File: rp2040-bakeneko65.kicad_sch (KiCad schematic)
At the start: 1 part

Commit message: Some schematic work
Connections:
- net +3V3: now reaches U?.1 (IOVDD), U?.10 (IOVDD), U?.22 (IOVDD), U?.33 (IOVDD), U?.42 (IOVDD), U?.49 (IOVDD)
- net +3V3: now also U?.43 (ADC_AVDD), U?.44 (VREG_IN), U?.48 (USB_VDD)
- net +1V1: now reaches U?.23 (DVDD), U?.50 (DVDD)
- net +1V1: now also U?.45 (VREG_VOUT)
- net SWCLK: now reaches U?.24 (SWCLK)
- net SWD: now reaches U?.25 (SWD)
- net SD3: now reaches U?.51 (QSPI_SD3)
- net QSPI_CLK: now reaches U?.52 (QSPI_SCLK)
- net SD0: now reaches U?.53 (QSPI_SD0)
- net SD2: now reaches U?.54 (QSPI_SD2)
- net SD1: now reaches U?.55 (QSPI_SD1)
- net CS: now reaches U?.56 (QSPI_SS)
- net GND: now reaches U?.57 (GND)
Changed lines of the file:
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@@
 (kicad_sch (version 20211123) (generator eeschema)
   (paper "A4")
+  (junction (at 81.28 29.21) (diameter 0) (color 0 0 0 0)
+  )
+  (junction (at 78.74 29.21) (diameter 0) (color 0 0 0 0)
+  )
+  (junction (at 76.2 29.21) (diameter 0) (color 0 0 0 0)
+  )
+  (junction (at 68.58 29.21) (diameter 0) (color 0 0 0 0)
+  )
+  (wire (pts (xy 76.2 29.21) (xy 78.74 29.21))
+    (stroke (width 0) (type default) (color 0 0 0 0))
+  )
+  (wire (pts (xy 76.2 26.67) (xy 76.2 29.21))
+    (stroke (width 0) (type default) (color 0 0 0 0))
+  )
+  (wire (pts (xy 69.85 120.65) (xy 73.66 120.65))
+    (stroke (width 0) (type default) (color 0 0 0 0))
+  )
+  (wire (pts (xy 78.74 29.21) (xy 81.28 29.21))
+    (stroke (width 0) (type default) (color 0 0 0 0))
+  )
+  (wire (pts (xy 68.58 29.21) (xy 71.12 29.21))
+    (stroke (width 0) (type default) (color 0 0 0 0))
+  )
+  (wire (pts (xy 81.28 29.21) (xy 83.82 29.21))
+    (stroke (width 0) (type default) (color 0 0 0 0))
+  )
+  (wire (pts (xy 68.58 26.67) (xy 68.58 29.21))
+    (stroke (width 0) (type default) (color 0 0 0 0))
+  )
+  (global_label "CS" (shape input) (at 48.26 54.61 180) (fields_autoplaced)
+    (effects (font (size 1.27 1.27)) (justify right))
+    (property "Intersheet References" "${INTERSHEET_REFS}" (id 0) (at 43.3674 54.5306 0)
+      (effects (font (size 1.27 1.27)) (justify right) hide)
+    )
+  )
+  (global_label "QSPI_CLK" (shape input) (at 48.26 69.85 180) (fields_autoplaced)
+    (effects (font (size 1.27 1.27)) (justify right))
+    (property "Intersheet References" "${INTERSHEET_REFS}" (id 0) (at 36.8964 69.7706 0)
+      (effects (font (size 1.27 1.27)) (justify right) hide)
+    )
+  )
+  (global_label "SWCLK" (shape input) (at 48.26 102.87 180) (fields_autoplaced)
+    (effects (font (size 1.27 1.27)) (justify right))
+    (property "Intersheet References" "${INTERSHEET_REFS}" (id 0) (at 39.6179 102.7906 0)
+      (effects (font (size 1.27 1.27)) (justify right) hide)
+    )
+  )
+  (global_label "SWD" (shape input) (at 48.26 105.41 180) (fields_autoplaced)
+    (effects (font (size 1.27 1.27)) (justify right))
+    (property "Intersheet References" "${INTERSHEET_REFS}" (id 0) (at 41.9159 105.3306 0)
+      (effects (font (size 1.27 1.27)) (justify right) hide)
+    )
+  )
+  (global_label "SD1" (shape input) (at 48.26 62.23 180) (fields_autoplaced)
+    (effects (font (size 1.27 1.27)) (justify right))
+    (property "Intersheet References" "${INTERSHEET_REFS}" (id 0) (at 42.1579 62.1506 0)
+      (effects (font (size 1.27 1.27)) (justify right) hide)
+    )
+  )
+  (global_label "SD2" (shape input) (at 48.26 64.77 180) (fields_autoplaced)
+    (effects (font (size 1.27 1.27)) (justify right))
+    (property "Intersheet References" "${INTERSHEET_REFS}" (id 0) (at 42.1579 64.6906 0)
+      (effects (font (size 1.27 1.27)) (justify right) hide)
+    )
+  )
+  (global_label "SD0" (shape input) (at 48.26 59.69 180) (fields_autoplaced)
+    (effects (font (size 1.27 1.27)) (justify right))
+    (property "Intersheet References" "${INTERSHEET_REFS}" (id 0) (at 42.1579 59.6106 0)
+      (effects (font (size 1.27 1.27)) (justify right) hide)
+    )
+  )
+  (global_label "SD3" (shape input) (at 48.26 67.31 180) (fields_autoplaced)
+    (effects (font (size 1.27 1.27)) (justify right))
+    (property "Intersheet References" "${INTERSHEET_REFS}" (id 0) (at 42.1579 67.2306 0)
+      (effects (font (size 1.27 1.27)) (justify right) hide)
+    )
+  )
+  (symbol (lib_id "power:GND") (at 69.85 120.65 0) (unit 1)
+    (in_bom yes) (on_board yes) (fields_autoplaced)
+    (property "Reference" "#PWR?" (id 0) (at 69.85 127 0)
+      (effects (font (size 1.27 1.27)) hide)
+    )
+    (property "Value" "GND" (id 1) (at 69.85 125.73 0))
+    (property "Footprint" "" (id 2) (at 69.85 120.65 0)
+      (effects (font (size 1.27 1.27)) hide)
+    )
+    (property "Datasheet" "" (id 3) (at 69.85 120.65 0)
+      (effects (font (size 1.27 1.27)) hide)
+    )
+    (pin "1")
+  )
+  (symbol (lib_id "power:+3V3") (at 76.2 26.67 0) (unit 1)
+    (in_bom yes) (on_board yes) (fields_autoplaced)
+    (property "Reference" "#PWR?" (id 0) (at 76.2 30.48 0)
+      (effects (font (size 1.27 1.27)) hide)
+    )
+    (property "Value" "+3V3" (id 1) (at 76.2 21.59 0))
+    (property "Footprint" "" (id 2) (at 76.2 26.67 0)
+      (effects (font (size 1.27 1.27)) hide)
+    )
+    (property "Datasheet" "" (id 3) (at 76.2 26.67 0)
+      (effects (font (size 1.27 1.27)) hide)
+    )
+    (pin "1")
+  )
   (symbol (lib_id "MCU_RaspberryPi:RP2040") (at 73.66 74.93 0) (unit 1)
     (in_bom yes) (on_board yes) (fields_autoplaced)
@@
     (pin "9")
   )
+  (symbol (lib_id "power:+1V1") (at 68.58 26.67 0) (unit 1)
+    (in_bom yes) (on_board yes) (fields_autoplaced)
+    (property "Reference" "#PWR?" (id 0) (at 68.58 30.48 0)
+      (effects (font (size 1.27 1.27)) hide)
+    )
+    (property "Value" "+1V1" (id 1) (at 68.58 21.59 0))
+    (property "Footprint" "" (id 2) (at 68.58 26.67 0)
+      (effects (font (size 1.27 1.27)) hide)
+    )
+    (property "Datasheet" "" (id 3) (at 68.58 26.67 0)
+      (effects (font (size 1.27 1.27)) hide)
+    )
+    (pin "1")
+  )
   (sheet_instances
     (path "/" (page "1"))
   )
   (symbol_instances
+    (path "/0429f72c-16b0-4744-90f4-bc022597ca0f"
+      (reference "#PWR?") (unit 1) (value "GND") (footprint "")
+    )
+    (path "/10a7cbd1-d76a-46cc-8e26-d9c6917c2458"
+      (reference "#PWR?") (unit 1) (value "+3V3") (footprint "")
+    )
+    (path "/7e675cbf-1df0-4184-8643-46226909b2bc"
+      (reference "#PWR?") (unit 1) (value "+1V1") (footprint "")
+    )
     (path "/7983fcb6-a16e-4782-bd80-c146df78a95c"
       (reference "U?") (unit 1) (value "RP2040") (footprint "Package_DFN_QFN:QFN-56-1EP_7x7mm_P0.4mm_EP3.2x3.2mm")

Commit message: MCU done
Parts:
- added R5, R6: 27, symbol Device:R_Small
- added R7: 10k, symbol Device:R_Small
- added SW?: SW_Push, symbol Switch:SW_Push
- gave numbers to parts that had none: 1
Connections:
- net GND: now also U3.19 (TESTEN), SW?.1
- net XTAL_IN: now reaches U3.20 (XIN)
- net XTAL_OUT: now reaches U3.21 (XOUT)
- net at U3.26 (RUN): now also R7.2, SW?.2
- net at U3.46 (USB_DM): now also R6.2
- net at U3.47 (USB_DP): now also R5.2
- new net +5V: R7.1
- new net D+: R5.1
- new net D-: R6.1
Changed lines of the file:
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@@
   (junction (at 76.2 29.21) (diameter 0) (color 0 0 0 0)
   )
+  (junction (at 46.99 36.83) (diameter 0) (color 0 0 0 0)
+  )
   (junction (at 68.58 29.21) (diameter 0) (color 0 0 0 0)
   )
@@
     (stroke (width 0) (type default) (color 0 0 0 0))
   )
+  (wire (pts (xy 45.72 82.55) (xy 48.26 82.55))
+    (stroke (width 0) (type default) (color 0 0 0 0))
+  )
   (wire (pts (xy 69.85 120.65) (xy 73.66 120.65))
     (stroke (width 0) (type default) (color 0 0 0 0))
@@
     (stroke (width 0) (type default) (color 0 0 0 0))
   )
+  (wire (pts (xy 46.99 31.75) (xy 46.99 36.83))
+    (stroke (width 0) (type default) (color 0 0 0 0))
+  )
+  (wire (pts (xy 34.29 35.56) (xy 30.48 35.56))
+    (stroke (width 0) (type default) (color 0 0 0 0))
+  )
+  (wire (pts (xy 43.18 44.45) (xy 48.26 44.45))
+    (stroke (width 0) (type default) (color 0 0 0 0))
+  )
+  (wire (pts (xy 34.29 36.83) (xy 34.29 35.56))
+    (stroke (width 0) (type default) (color 0 0 0 0))
+  )
+  (wire (pts (xy 45.72 92.71) (xy 48.26 92.71))
+    (stroke (width 0) (type default) (color 0 0 0 0))
+  )
+  (wire (pts (xy 34.29 46.99) (xy 38.1 46.99))
+    (stroke (width 0) (type default) (color 0 0 0 0))
+  )
   (wire (pts (xy 68.58 29.21) (xy 71.12 29.21))
     (stroke (width 0) (type default) (color 0 0 0 0))
   )
+  (wire (pts (xy 34.29 44.45) (xy 38.1 44.45))
+    (stroke (width 0) (type default) (color 0 0 0 0))
+  )
+  (wire (pts (xy 46.99 24.13) (xy 46.99 26.67))
+    (stroke (width 0) (type default) (color 0 0 0 0))
+  )
+  (wire (pts (xy 46.99 36.83) (xy 48.26 36.83))
+    (stroke (width 0) (type default) (color 0 0 0 0))
+  )
+  (wire (pts (xy 43.18 113.03) (xy 48.26 113.03))
+    (stroke (width 0) (type default) (color 0 0 0 0))
+  )
   (wire (pts (xy 81.28 29.21) (xy 83.82 29.21))
     (stroke (width 0) (type default) (color 0 0 0 0))
   )
+  (wire (pts (xy 43.18 46.99) (xy 48.26 46.99))
+    (stroke (width 0) (type default) (color 0 0 0 0))
+  )
   (wire (pts (xy 68.58 26.67) (xy 68.58 29.21))
     (stroke (width 0) (type default) (color 0 0 0 0))
   )
+  (wire (pts (xy 44.45 36.83) (xy 46.99 36.83))
+    (stroke (width 0) (type default) (color 0 0 0 0))
+  )
+  (global_label "XTAL_OUT" (shape input) (at 45.72 92.71 180) (fields_autoplaced)
+    (effects (font (size 1.27 1.27)) (justify right))
+    (property "Intersheet References" "${INTERSHEET_REFS}" (id 0) (at 34.4169 92.6306 0)
+      (effects (font (size 1.27 1.27)) (justify right) hide)
+    )
+  )
+  (global_label "XTAL_IN" (shape input) (at 45.72 82.55 180) (fields_autoplaced)
+    (effects (font (size 1.27 1.27)) (justify right))
+    (property "Intersheet References" "${INTERSHEET_REFS}" (id 0) (at 36.1102 82.4706 0)
+      (effects (font (size 1.27 1.27)) (justify right) hide)
+    )
+  )
   (global_label "CS" (shape input) (at 48.26 54.61 180) (fields_autoplaced)
     (effects (font (size 1.27 1.27)) (justify right))
@@
     )
   )
+  (global_label "D-" (shape input) (at 34.29 46.99 180) (fields_autoplaced)
+    (effects (font (size 1.27 1.27)) (justify right))
+    (property "Intersheet References" "${INTERSHEET_REFS}" (id 0) (at 29.0345 46.9106 0)
+      (effects (font (size 1.27 1.27)) (justify right) hide)
+    )
+  )
   (global_label "SWCLK" (shape input) (at 48.26 102.87 180) (fields_autoplaced)
     (effects (font (size 1.27 1.27)) (justify right))
@@
     (effects (font (size 1.27 1.27)) (justify right))
     (property "Intersheet References" "${INTERSHEET_REFS}" (id 0) (at 42.1579 67.2306 0)
+      (effects (font (size 1.27 1.27)) (justify right) hide)
+    )
+  )
+  (global_label "D+" (shape input) (at 34.29 44.45 180) (fields_autoplaced)
+    (effects (font (size 1.27 1.27)) (justify right))
+    (property "Intersheet References" "${INTERSHEET_REFS}" (id 0) (at 29.0345 44.3706 0)
       (effects (font (size 1.27 1.27)) (justify right) hide)
     )
@@
     (pin "1")
   )
+  (symbol (lib_id "power:GND") (at 30.48 35.56 0) (unit 1)
+    (in_bom yes) (on_board yes) (fields_autoplaced)
+    (property "Reference" "#PWR?" (id 0) (at 30.48 41.91 0)
+      (effects (font (size 1.27 1.27)) hide)
+    )
+    (property "Value" "GND" (id 1) (at 30.48 40.64 0))
+    (property "Footprint" "" (id 2) (at 30.48 35.56 0)
+      (effects (font (size 1.27 1.27)) hide)
+    )
+    (property "Datasheet" "" (id 3) (at 30.48 35.56 0)
+      (effects (font (size 1.27 1.27)) hide)
+    )
+    (pin "1")
+  )
+  (symbol (lib_id "power:+5V") (at 46.99 24.13 0) (unit 1)
+    (in_bom yes) (on_board yes) (fields_autoplaced)
+    (property "Reference" "#PWR?" (id 0) (at 46.99 27.94 0)
+      (effects (font (size 1.27 1.27)) hide)
+    )
+    (property "Value" "+5V" (id 1) (at 46.99 19.05 0))
+    (property "Footprint" "" (id 2) (at 46.99 24.13 0)
+      (effects (font (size 1.27 1.27)) hide)
+    )
+    (property "Datasheet" "" (id 3) (at 46.99 24.13 0)
+      (effects (font (size 1.27 1.27)) hide)
+    )
+    (pin "1")
+  )
+  (symbol (lib_id "power:GND") (at 43.18 113.03 0) (unit 1)
+    (in_bom yes) (on_board yes) (fields_autoplaced)
+    (property "Reference" "#PWR?" (id 0) (at 43.18 119.38 0)
+      (effects (font (size 1.27 1.27)) hide)
+    )
+    (property "Value" "GND" (id 1) (at 43.18 118.11 0))
+    (property "Footprint" "" (id 2) (at 43.18 113.03 0)
+      (effects (font (size 1.27 1.27)) hide)
+    )
+    (property "Datasheet" "" (id 3) (at 43.18 113.03 0)
+      (effects (font (size 1.27 1.27)) hide)
+    )
+    (pin "1")
+  )
   (symbol (lib_id "MCU_RaspberryPi:RP2040") (at 73.66 74.93 0) (unit 1)
     (in_bom yes) (on_board yes) (fields_autoplaced)
-    (property "Reference" "U?" (id 0) (at 75.6794 119.38 0)
+    (property "Reference" "U3" (id 0) (at 75.6794 119.38 0)
       (effects (font (size 1.27 1.27)) (justify left))
     )
@@
     (pin "1")
   )
+  (symbol (lib_id "Switch:SW_Push") (at 39.37 36.83 0) (unit 1)
+    (in_bom yes) (on_board yes) (fields_autoplaced)
+    (property "Reference" "SW?" (id 0) (at 39.37 29.21 0))
+    (property "Value" "SW_Push" (id 1) (at 39.37 31.75 0))
+    (property "Footprint" "" (id 2) (at 39.37 31.75 0)
+      (effects (font (size 1.27 1.27)) hide)
+    )
+    (property "Datasheet" "~" (id 3) (at 39.37 31.75 0)
+      (effects (font (size 1.27 1.27)) hide)
+    )
+    (pin "1")
+    (pin "2")
+  )
+  (symbol (lib_id "Device:R_Small") (at 46.99 29.21 0) (unit 1)
+    (in_bom yes) (on_board yes) (fields_autoplaced)
+    (property "Reference" "R7" (id 0) (at 49.53 27.9399 0)
+      (effects (font (size 1.27 1.27)) (justify left))
+    )
+    (property "Value" "10k" (id 1) (at 49.53 30.4799 0)
+      (effects (font (size 1.27 1.27)) (justify left))
+    )
+    (property "Footprint" "" (id 2) (at 46.99 29.21 0)
+      (effects (font (size 1.27 1.27)) hide)
+    )
+    (property "Datasheet" "~" (id 3) (at 46.99 29.21 0)
+      (effects (font (size 1.27 1.27)) hide)
+    )
+    (pin "1")
+    (pin "2")
+  )
+  (symbol (lib_id "Device:R_Small") (at 40.64 44.45 90) (unit 1)
+    (in_bom yes) (on_board yes)
+    (property "Reference" "R5" (id 0) (at 36.83 43.18 90))
+    (property "Value" "27" (id 1) (at 44.45 45.72 90))
+    (property "Footprint" "" (id 2) (at 40.64 44.45 0)
+      (effects (font (size 1.27 1.27)) hide)
+    )
+    (property "Datasheet" "~" (id 3) (at 40.64 44.45 0)
+      (effects (font (size 1.27 1.27)) hide)
+    )
+    (pin "1")
+    (pin "2")
+  )
+  (symbol (lib_id "Device:R_Small") (at 40.64 46.99 90) (unit 1)
+    (in_bom yes) (on_board yes)
+    (property "Reference" "R6" (id 0) (at 36.83 45.72 90))
+    (property "Value" "27" (id 1) (at 44.45 43.18 90))
+    (property "Footprint" "" (id 2) (at 40.64 46.99 0)
+      (effects (font (size 1.27 1.27)) hide)
+    )
+    (property "Datasheet" "~" (id 3) (at 40.64 46.99 0)
+      (effects (font (size 1.27 1.27)) hide)
+    )
+    (pin "1")
+    (pin "2")
+  )
   (sheet_instances
     (path "/" (page "1"))
@@
       (reference "#PWR?") (unit 1) (value "+3V3") (footprint "")
     )
+    (path "/16d0bbea-7a97-44ba-9618-50b5a25403d3"
+      (reference "#PWR?") (unit 1) (value "GND") (footprint "")
+    )
+    (path "/3e5a2547-57b3-4a9e-9065-53acd4f5fef1"
+      (reference "#PWR?") (unit 1) (value "+5V") (footprint "")
+    )
+    (path "/43560f97-a5bd-4807-9e3e-e7f802e75114"
+      (reference "#PWR?") (unit 1) (value "GND") (footprint "")
+    )
     (path "/7e675cbf-1df0-4184-8643-46226909b2bc"
       (reference "#PWR?") (unit 1) (value "+1V1") (footprint "")
     )
+    (path "/e82e7d2b-ad35-4be9-a59e-016eb5a2e0c6"
+      (reference "R5") (unit 1) (value "27") (footprint "")
+    )
+    (path "/f53f0ad2-5a69-42c2-bd3c-85dba572b511"
+      (reference "R6") (unit 1) (value "27") (footprint "")
+    )
+    (path "/b4641284-daf5-4245-88d0-5b4ce77cecf6"
+      (reference "R7") (unit 1) (value "10k") (footprint "")
+    )
+    (path "/9769ce52-6e73-4db2-bb86-cd67bfc206bf"
+      (reference "SW?") (unit 1) (value "SW_Push") (footprint "")
+    )
     (path "/7983fcb6-a16e-4782-bd80-c146df78a95c"
-      (reference "U?") (unit 1) (value "RP2040") (footprint "Package_DFN_QFN:QFN-56-1EP_7x7mm_P0.4mm_EP3.2x3.2mm")
-    )
-  )
+      (reference "U3") (unit 1) (value "RP2040") (footprint "Package_DFN_QFN:QFN-56-1EP_7x7mm_P0.4mm_EP3.2x3.2mm")
+    )
+  )

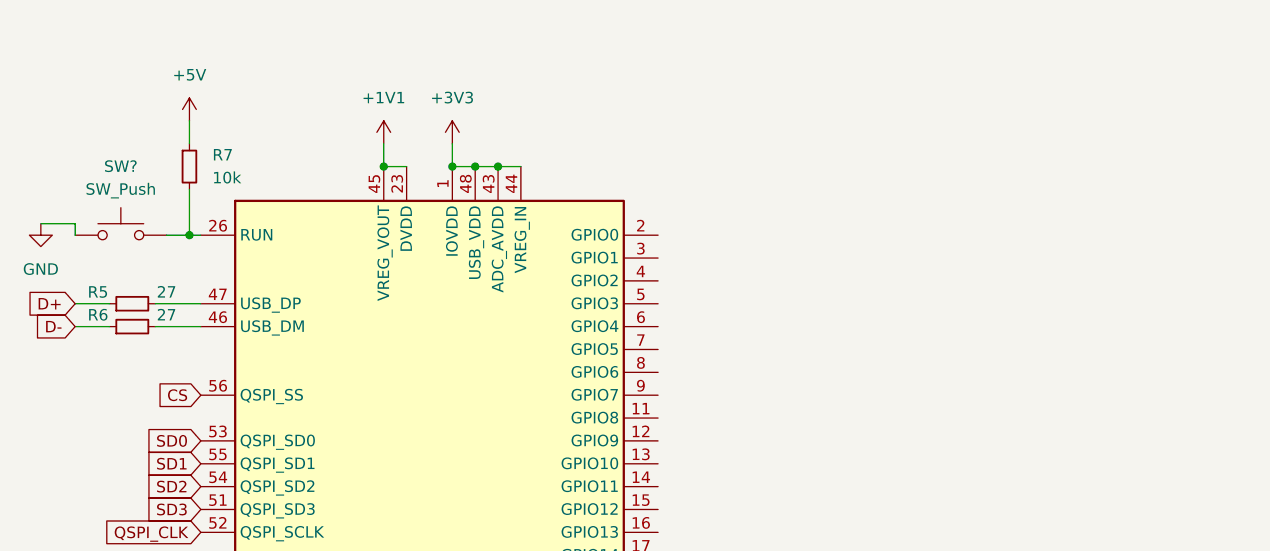
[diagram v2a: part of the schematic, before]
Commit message: Add flash
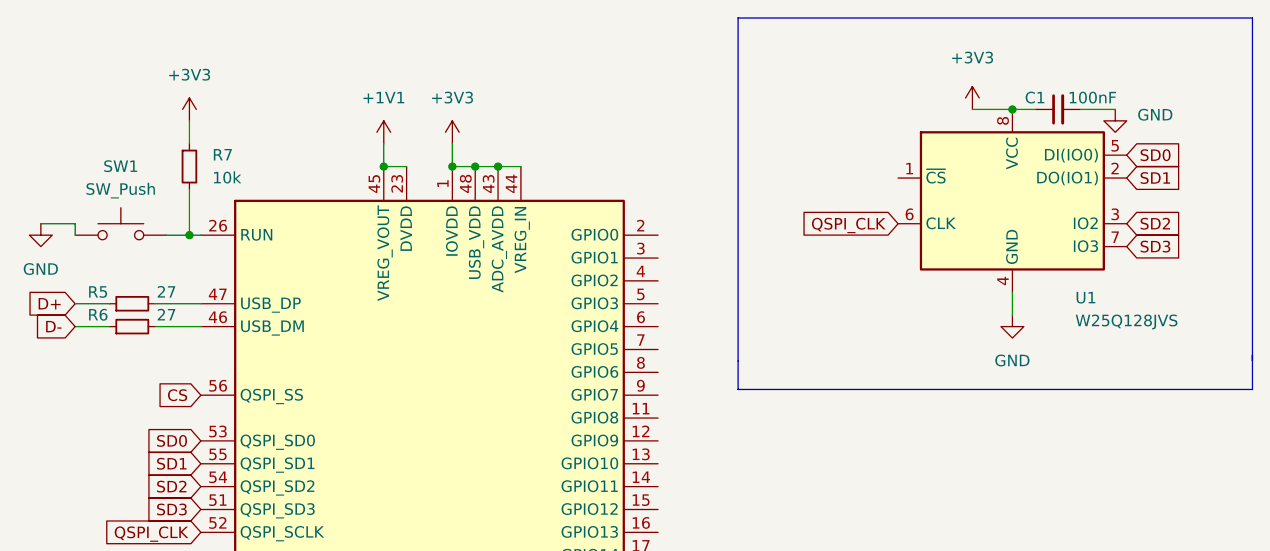
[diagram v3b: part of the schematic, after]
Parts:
- added C1: 100nF, symbol Device:C_Small
- added U1: W25Q128JVS, Package_SO:SOIC-8_5.23x5.23mm_P1.27mm, symbol Memory_Flash:W25Q128JVS
- gave numbers to parts that had none: 1
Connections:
- net +5V is gone; now on net +3V3: R7.1
- net +3V3: now also C1.1, U1.8 (VCC)
- net GND: now also C1.2, U1.4 (GND)
- net QSPI_CLK: now also U1.6 (CLK)
- net SD0: now also U1.5 (DI(IO0))
- net SD1: now also U1.2 (DO(IO1))
- net SD2: now also U1.3 (IO2)
- net SD3: now also U1.7 (IO3)
